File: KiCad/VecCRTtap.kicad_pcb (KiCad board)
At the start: 2 copper layers, 30 parts, among them J1 Conn_02x08_Top_Bottom, J2 Conn_02x08_Top_Bottom, J3 X, J4 Y, J5 Z, K1 KLINKE_3POL, K2 1UM, Q1 BS250, Q2 BS170

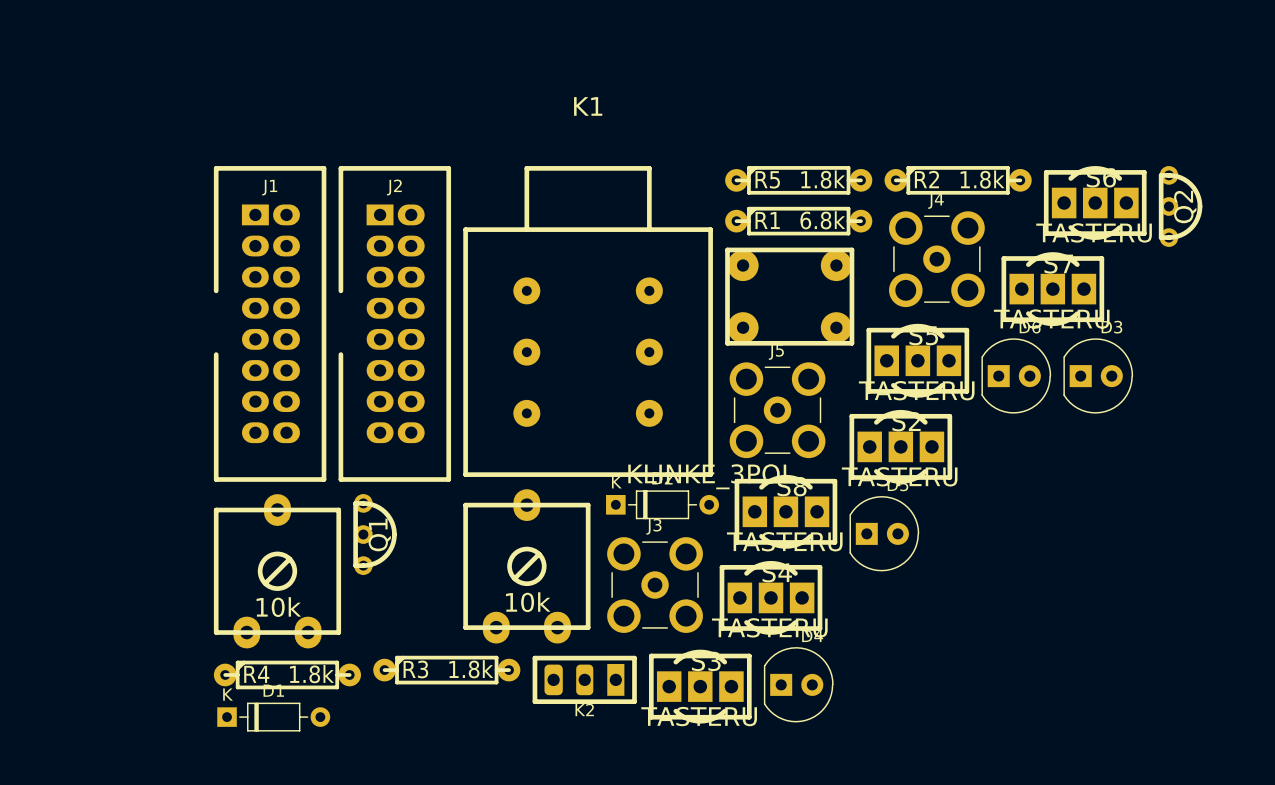
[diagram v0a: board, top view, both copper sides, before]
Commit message: revise tap board
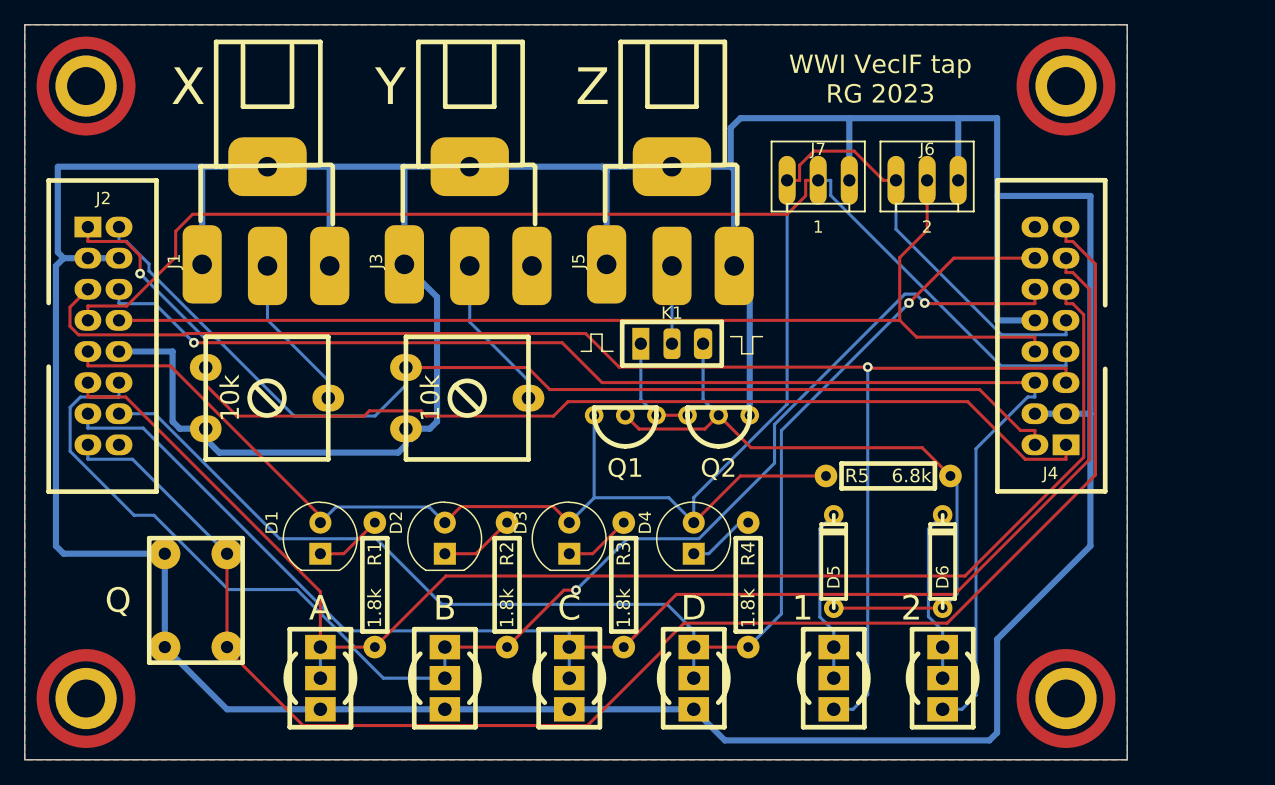
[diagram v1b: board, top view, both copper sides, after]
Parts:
- removed the D5 at (70.0, 41.6)
- removed the D6 at (80.8, 28.7)
- removed the J1 at (18.8, 15.5)
- removed the K1 at (46.0, 26.7)
- removed the S5 at (72.9, 27.4)
- added D1: LED, RG:LED_D5.0mm, F.Cu at (24.1, 41.9)
- added D2: LED, RG:LED_D5.0mm, F.Cu at (34.3, 41.9)
- added J4: Conn_02x08_Odd_Even, RG:Wannenstecker_2x08_V, F.Cu at (85.0, 34.3)
- added J6: Conn_01x03, RG:PSS_3, F.Cu at (73.7, 12.7)
- added J7: Conn_01x03, RG:PSS_3, F.Cu at (64.8, 12.7)
- added Y1: 3mm, RG:Bohrloch3mm, F.Cu at (85.0, 55.0)
- added Y2: 3mm, RG:Bohrloch3mm, F.Cu at (5.00, 55.0)
- added Y3: 3mm, RG:Bohrloch3mm, F.Cu at (85.0, 5.00)
- added Y4: 3mm, RG:Bohrloch3mm, F.Cu at (5.00, 5.00)
- D5: renamed from D1; footprint Diode_THT:D_DO-35_SOD27_P7.62mm_Horizontal -> RG:D3
- D6: renamed from D2; footprint Diode_THT:D_DO-35_SOD27_P7.62mm_Horizontal -> RG:D3
- J1: renamed from J3; footprint Connector_Coaxial:SMB_Jack_Vertical -> RG:Cinch_liegend
- J2: value Conn_02x08_Top_Bottom -> Conn_02x08_Odd_Even
- J3: renamed from J4; footprint Connector_Coaxial:SMB_Jack_Vertical -> RG:Cinch_liegend
- J5: footprint Connector_Coaxial:SMB_Jack_Vertical -> RG:Cinch_liegend
- moved R1 57.9 mm to (28.6, 45.7), turned to -90 degrees
- moved S5 54.5 mm to (14.0, 47.0), turned to -90 degrees
- moved S1 51.0 mm to (24.1, 53.3), turned to -90 degrees
- moved D5 50.8 mm to (66.0, 45.1), turned to 90 degrees
- moved S4 50.8 mm to (54.6, 53.3), turned to -90 degrees
- moved D3 45.0 mm to (44.5, 41.9), turned to 90 degrees
- moved J1 41.0 mm to (19.8, 19.7), turned to 90 degrees
- moved Q2 40.5 mm to (56.6, 31.9), turned to -90 degrees
- moved J3 38.1 mm to (36.3, 19.7), turned to 90 degrees
- moved S6 36.5 mm to (66.0, 53.3), turned to -90 degrees
- moved R4 33.3 mm to (59.1, 45.7), turned to -90 degrees
- moved R3 28.4 mm to (48.9, 45.7), turned to -90 degrees
- moved K1 28.4 mm to (52.8, 26.0), turned to 180 degrees
- moved D6 27.3 mm to (74.9, 45.1), turned to 90 degrees
- moved J2 23.9 mm to (5.15, 16.5)
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- renumbered K2 to K1, R2 to R1, R3 to R2, R4 to R3, R5 to R4, R1 to R5, S2 to S1, S3 to S2, S4 to S3, S6 to S4, S1 to S5, S7 to S6, S8 to S7
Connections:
- D5 pad 1: Net-(D1-Pad1) -> Net-(S6-Pad1)
- D6 pad 1: Net-(D2-Pad1) -> Net-(S7-Pad1)
- J2 pad 11: /Z2 -> /GPIO5
- J2 pad 12: /gun2 -> /GPIO6
- J2 pad 13: GND -> /GPIO20
- J2 pad 14: /GPIO6 -> /GPIO21
- J2 pad 15: /GPIO21 -> /isKEY
- J2 pad 2: GND -> /Yout
- J2 pad 3: /Z1 -> GND
- J2 pad 4: /gun1 -> GND
- J2 pad 5: +5V -> /Z1
- J2 pad 6: /GPIO5 -> /Z2
- J2 pad 7: /GPIO20 -> /gun1
- J2 pad 8: /isKEY -> /gun2
- J2 pad 9: /Yout -> +5V
- R1 pad 1: +5V -> Net-(R1-Pad1)
- R1 pad 2: Net-(D3-PadA) -> /GPIO5
- R2 pad 1: +5V -> Net-(R2-Pad1)
- R2 pad 2: Net-(D4-PadA) -> /GPIO6
- R3 pad 1: +5V -> Net-(R3-Pad1)
- R3 pad 2: Net-(D5-PadA) -> /GPIO20
- R4 pad 1: +5V -> Net-(R4-Pad1)
- R4 pad 2: Net-(D6-PadA) -> /GPIO21
- S1 pad 1: unconnected-(S2-Pad1) -> /GPIO5
- S2 pad 1: unconnected-(S3-Pad1) -> /GPIO6
- S3 pad 1: unconnected-(S4-Pad1) -> /GPIO20
- S4 pad 1: unconnected-(S6-Pad1) -> /GPIO21
- S6 pad 1: unconnected-(S7-Pad1) -> Net-(S6-Pad1)
- S6 pad 2: Net-(D1-Pad1) -> Net-(S6-Pad1)
- S6 pad 3: /z1 -> /Z1
- S7 pad 1: unconnected-(S8-Pad1) -> Net-(S7-Pad1)
- S7 pad 2: Net-(D2-Pad1) -> Net-(S7-Pad1)
- S7 pad 3: /z2 -> /Z2
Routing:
- net GND: track 0.00 -> 394.4 mm
- net +5V: track 0.00 -> 144.5 mm
- net /isKEY: track 0.00 -> 127.3 mm
- net /Z1: track 0.00 -> 117.6 mm, vias 0 -> 1
- net /GPIO20: track 0.00 -> 117.6 mm
- net /GPIO5: track 0.00 -> 117.2 mm
- net /GPIO6: track 0.00 -> 113.5 mm, vias 0 -> 2
- net /Z2: track 0.00 -> 109.7 mm, vias 0 -> 1
- net /GPIO21: track 0.00 -> 107.9 mm, vias 0 -> 1
- net /gun1: track 0.00 -> 95.4 mm
- net /Xout: track 0.00 -> 93.9 mm, vias 0 -> 1
- net /gun2: track 0.00 -> 88.9 mm
- net /Yout: track 0.00 -> 88.0 mm
- net Net-(D5-Pad2): track 0.00 -> 56.3 mm
- net Net-(S7-Pad1): track 0.00 -> 14.3 mm
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- added copper zone on F.Cu, net (none)
- added copper zone on B.Cu, net GND
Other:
- board outline added: 90 x 60 mm
- board text added: "1"
- board text added: "2"
- board text added: "A"
- board text added: "B"
- board text added: "C"
- board text added: "D"
- board text added: "Q"
- board text added: "WWI VecIF tap RG 2023"
- board text added: "X"
- board text added: "Y"
- board text added: "Z"

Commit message: Enlarge board, larger PB
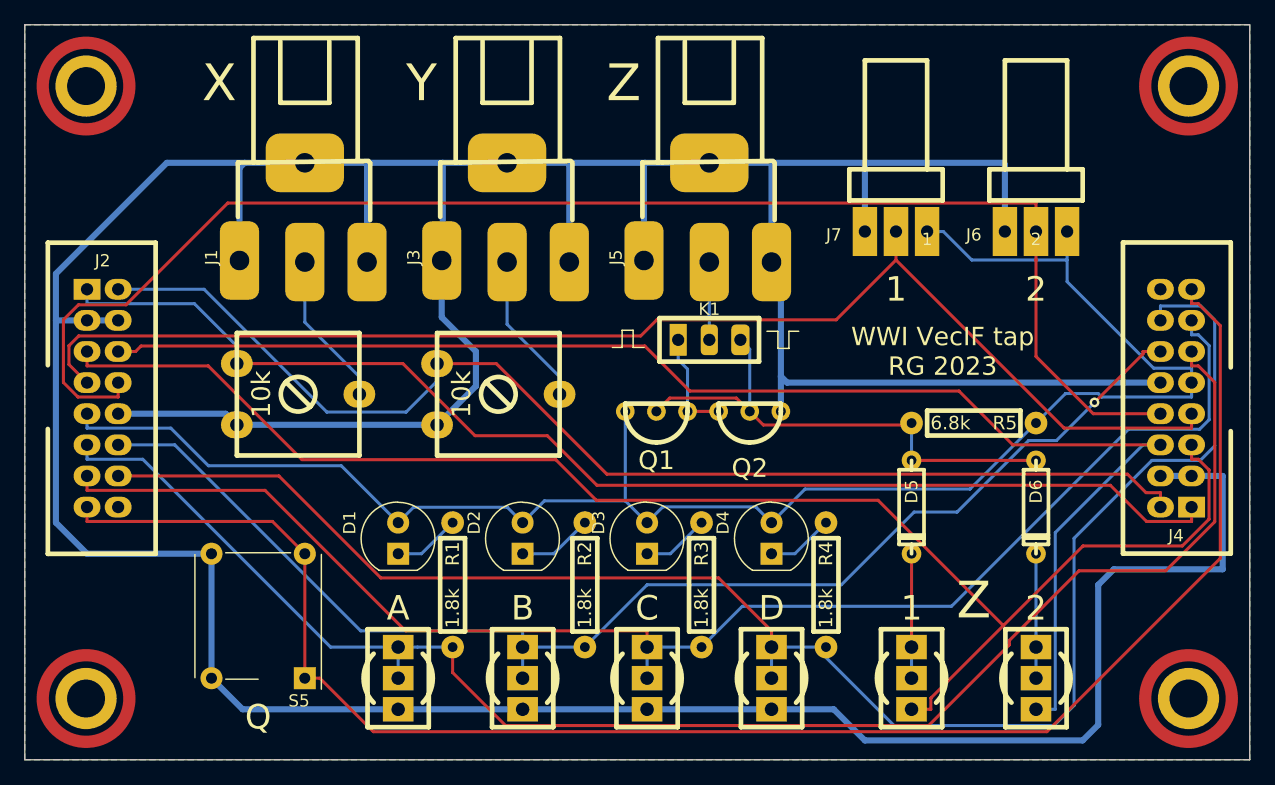
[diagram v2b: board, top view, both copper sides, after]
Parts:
- J6, J7: footprint RG:PSS_3 -> RG:PSS_3W
- S5: footprint RG:Tast2mil -> Button_Switch_THT:SW_MEC_5GTH9
- moved J4 11.4 mm to (95.2, 39.4)
- moved S5 10.9 mm to (22.9, 53.3), turned to 180 degrees
- moved D6 10.3 mm to (82.5, 38.1), turned to -90 degrees
- moved Y1 10.0 mm to (95.0, 55.0)
- moved Y3 10.0 mm to (95.0, 5.00)
- moved J6 9.82 mm to (82.5, 16.9), turned to 0 degrees
- moved D5 9.44 mm to (72.4, 38.1), turned to -90 degrees
- moved R5 8.21 mm to (77.5, 32.5), turned to 180 degrees
- moved S7 7.62 mm to (82.5, 53.3)
- moved J7 7.60 mm to (71.1, 16.9), turned to 0 degrees
- moved D1 6.35 mm to (30.5, 41.9)
- moved D2 6.35 mm to (40.6, 41.9)
- moved D4 6.35 mm to (61.0, 41.9)
- moved R2 6.35 mm to (45.7, 45.7)
- moved R4 6.35 mm to (65.4, 45.7)
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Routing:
- net /gun2: track 88.9 -> 119.2 mm
- net /GPIO21: track 107.9 -> 135.6 mm, vias 1 -> 0
- net Net-(D5-Pad2): track 56.3 -> 41.6 mm
- net /gun1: track 95.4 -> 107.4 mm
- net /GPIO5: track 117.2 -> 128.1 mm
- net /Yout: track 88.0 -> 97.3 mm
- net /isKEY: track 127.3 -> 135.9 mm
- net GND: track 394.4 -> 386.2 mm
- net /GPIO6: track 113.5 -> 105.4 mm, vias 2 -> 1
- net /Xout: track 93.9 -> 100.7 mm, vias 1 -> 0
- net /Z2: track 109.7 -> 116.2 mm, vias 1 -> 0
- net /Z1: track 117.6 -> 123.0 mm, vias 1 -> 0
- net Net-(S7-Pad1): track 14.3 -> 10.2 mm
- net Net-(S6-Pad1): track 14.3 -> 10.2 mm
- net +5V: track 144.5 -> 141.8 mm
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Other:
- board size 90 x 60 mm -> 100 x 60 mm

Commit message: Update lightgun LED, add HV, fixes
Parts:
- J6, J7: footprint RG:PSS_3W -> RG:PSS_3
- Q1: footprint RG:FETsgd_inline -> RG:FETdgs_inline
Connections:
- Q1 pad D: +5V -> Net-(K1-Pad3)
- Q1 pad S: Net-(K1-Pad3) -> +5V

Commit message: small fixes
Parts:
- J6, J7: footprint RG:PSS_3 -> RG:PSS_3W
- Q2: footprint RG:FETsgd_inline -> RG:FETdgs_inline
- moved K1 2.22 mm to (55.9, 27.9)
- moved Q2 1.90 mm to (59.2, 33.5), turned to 90 degrees
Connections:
- RV1 pad 1: /Xout -> GND
- RV1 pad 3: GND -> /Xout
- RV2 pad 1: /Yout -> GND
- RV2 pad 3: GND -> /Yout
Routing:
- net GND: track 386.2 -> 425.9 mm
- net +5V: track 141.8 -> 168.7 mm, vias 0 -> 1
- net /Z2: track 116.2 -> 134.1 mm, vias 0 -> 1
- net /gun2: track 119.2 -> 104.6 mm, vias 0 -> 2
- net /GPIO5: track 128.1 -> 142.6 mm
- net /isKEY: track 135.9 -> 148.0 mm
- net /Z1: track 123.0 -> 133.8 mm
- net /GPIO6: track 105.4 -> 115.8 mm
- net /gun1: track 107.4 -> 117.1 mm, vias 0 -> 1
- net /Xout: track 100.7 -> 109.7 mm, vias 0 -> 3
- net /GPIO21: track 135.6 -> 131.4 mm
- net /Yout: track 97.3 -> 94.3 mm, vias 0 -> 1
- net Net-(J5-Pad1): track 6.35 -> 8.57 mm
- net Net-(K1-Pad3): track 8.70 -> 7.26 mm
- net /GPIO20: track 118.1 -> 116.9 mm
